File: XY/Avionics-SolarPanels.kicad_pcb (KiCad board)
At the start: 4 copper layers, 82 x 100 mm, 206 parts, among them J1 200528-0100, J2 200528-0100, Q1 IRLML2803, Q17 NX3008NBKS, Q18 MBT2222ADW1T1, Q19 NX3008NBKS, Q2 SiRA99DP, Q20 MBT2222ADW1T1, Q21 NX3008NBKS, Q22 MBT2222ADW1T1, Q23 NX3008NBKS, Q24 MBT2222ADW1T1, Q25 NX3008NBKS, Q26 MBT2222ADW1T1, Q3 SiRA99DP, Q4 SiRA99DP, Q5 SiRA99DP, Q7 NX3008NBKS, Q8 MBT2222ADW1T1, U1 LTC4412xS6, U10 LTC3130, U11 LTC3130, U12 LTC3130, U13 ADM1176-1ARMZ-R7, U2 DRV8235RTER, U4 LTC4412xS6, U5 OPT4003DNPRQ1, U6 USBLC6-2P6, U8 LTC4412xS6

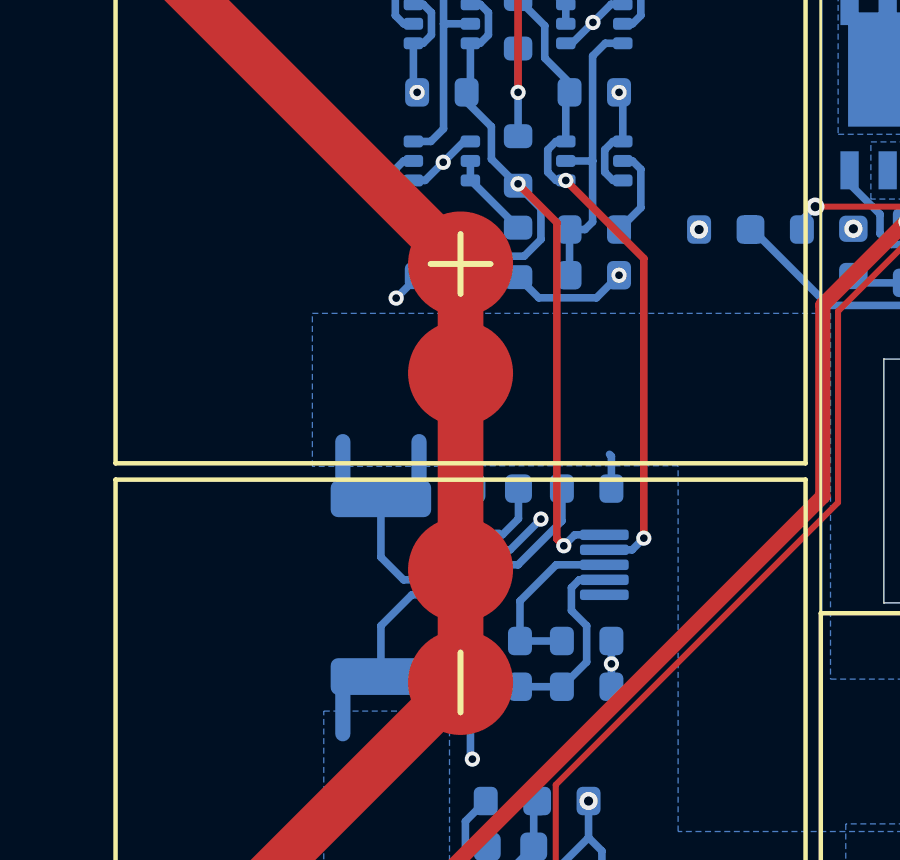
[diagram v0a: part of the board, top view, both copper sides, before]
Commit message: Added fusing to power monitor
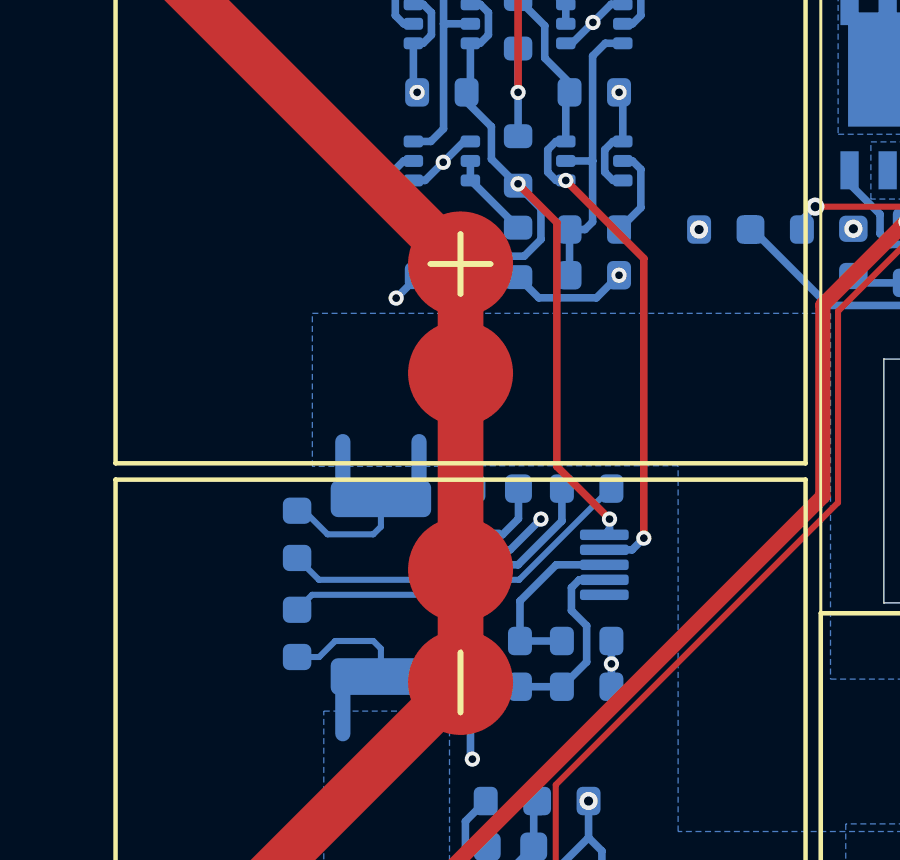
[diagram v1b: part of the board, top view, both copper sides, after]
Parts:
- added F10: 100mA, Fuse:Fuse_0603_1608Metric, B.Cu at (123.4, 104.6)
- added F9: 100mA, Fuse:Fuse_0603_1608Metric, B.Cu at (123.4, 108.0)
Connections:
- R125 pad 1: /Solar Charger/VCHRG -> Net-(U13-SENSE)
- U13 pad 1: VBATT -> Net-(U13-VCC)
- U13 pad 2: /Solar Charger/VCHRG -> Net-(U13-SENSE)
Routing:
- net Net-(U13-SENSE): track 0.00 -> 12.0 mm
- net Net-(U13-VCC): track 0.00 -> 6.22 mm
- net /Solar Charger/VCHRG: track 10.4 -> 8.44 mm
- net VBATT: track 58.5 -> 57.2 mm
- net /Solar Charger/I2C Single Protection5/DEVICE: track 27.2 -> 26.0 mm

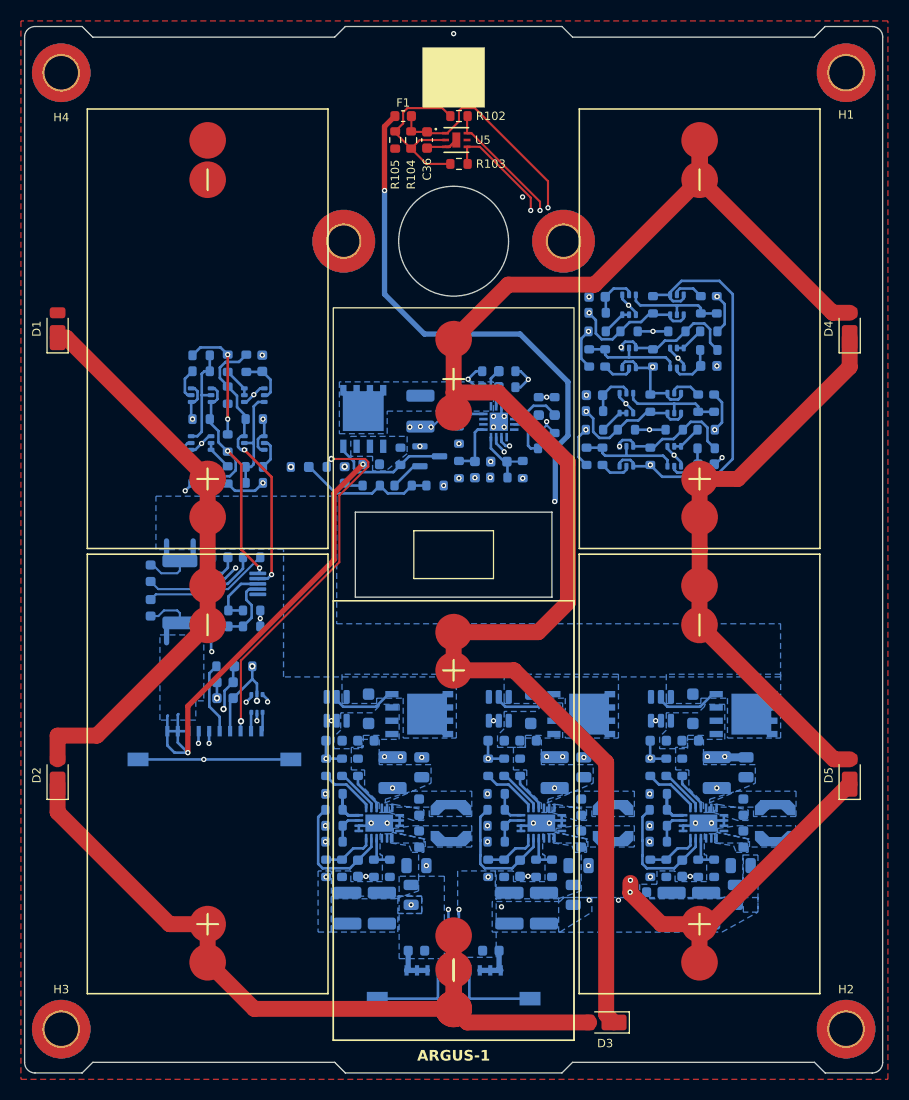
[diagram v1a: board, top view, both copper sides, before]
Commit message: Updated silkscreen and part number for solar panel bypass
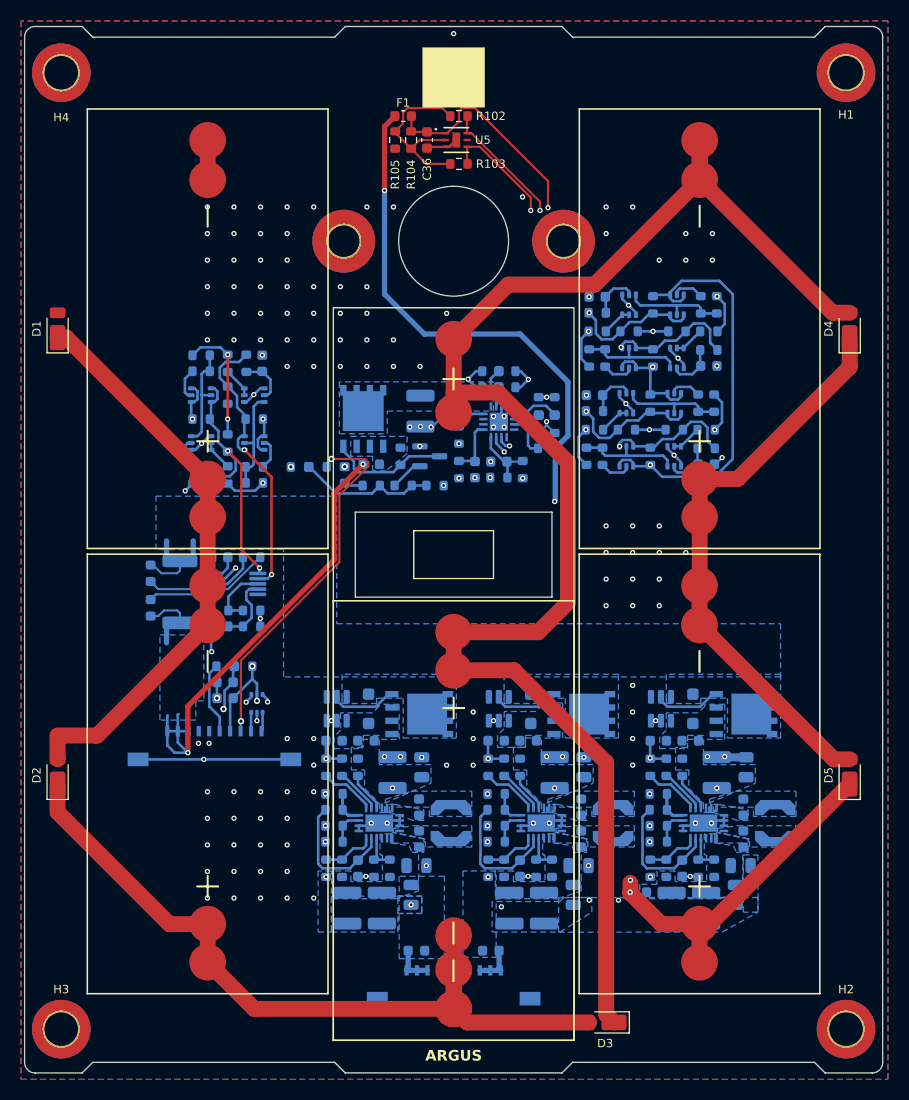
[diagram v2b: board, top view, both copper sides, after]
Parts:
- D1, D2, D3, D4, D5: value DFLS130L-7 -> DFLS130LQ-7
- SC1, SC2, SC4, SC5, SC6: value SM141K06TF -> SM141K06L
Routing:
- net GND: track 125.9 -> 93.6 mm, vias 76 -> 172
- added copper zone on In2.Cu, net GND
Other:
- board text added: "ARGUS"
- board text added: "D1 PWR"
- board text added: "D2 PWR"
- board text added: "XY PWR"
- board text removed: "ARGUS-1"
